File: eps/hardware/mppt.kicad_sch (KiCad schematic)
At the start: 1 part, among them U1 LTC3130IUDC_PBF

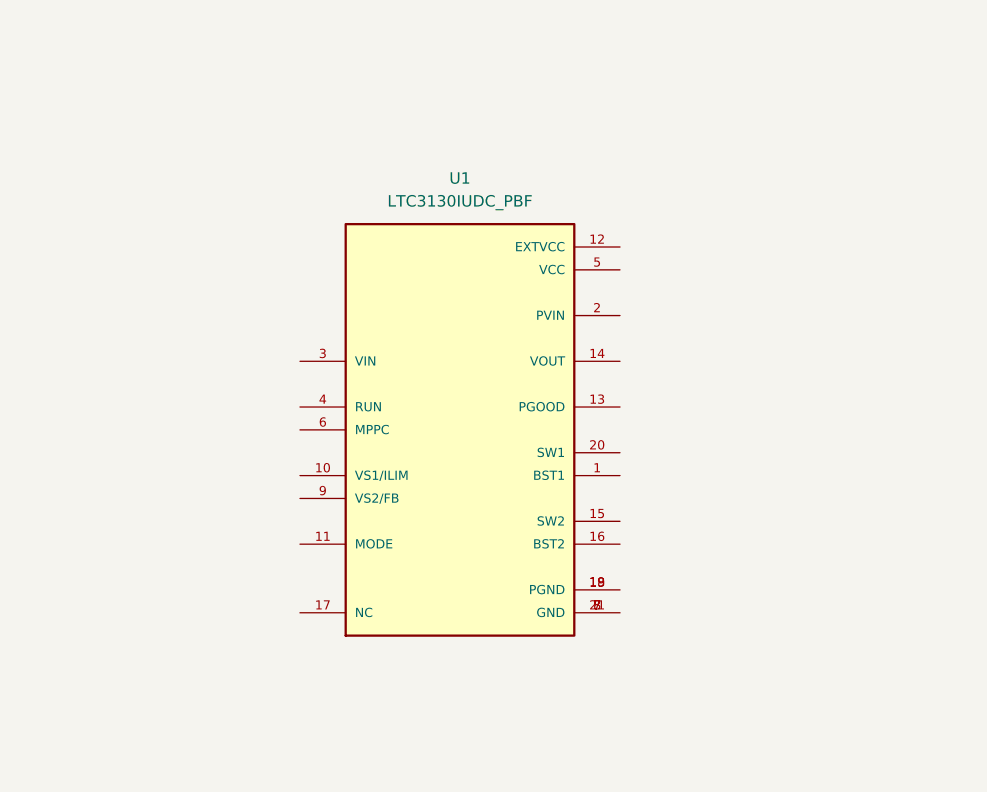
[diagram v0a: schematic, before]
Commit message: begin implementing battery charger
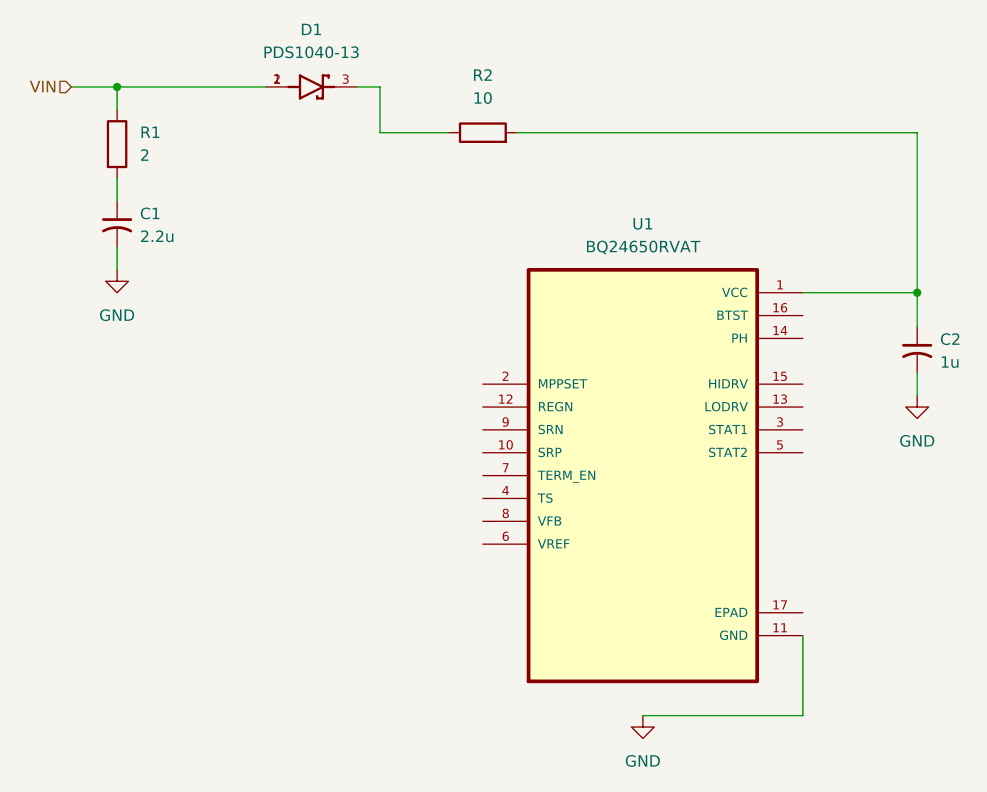
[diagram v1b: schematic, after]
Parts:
- removed U1: LTC3130IUDC_PBF, LTC3130IUDC_PBF:QFN50P400X300X80-21N, symbol LTC3130IUDC_PBF:LTC3130IUDC_PBF
- added C1: 2.2u, Capacitor_SMD:C_0603_1608Metric_Pad1.08x0.95mm_HandSolder, symbol Device:C_Small_US
- added C2: 1u, Capacitor_SMD:C_0603_1608Metric_Pad1.08x0.95mm_HandSolder, symbol Device:C_Small_US
- added D1: PDS1040-13, PDS1040-13:DIO_PDS1040-13, symbol PDS1040-13:PDS1040-13
- added R1: 2, Resistor_SMD:R_0603_1608Metric_Pad0.98x0.95mm_HandSolder, symbol Device:R
- added R2: 10, Resistor_SMD:R_0603_1608Metric_Pad0.98x0.95mm_HandSolder, symbol Device:R
- added U1: BQ24650RVAT, BQ24650RVAT:QFN50P350X350X100-17N, symbol BQ24650RVAT:BQ24650RVAT
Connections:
- new net: C1.1, R1.2
- new net: C2.1, R2.2, U1.1 (VCC)
- new net: D1.3, R2.1
- new net GND: C1.2, C2.2, U1.11 (GND)
- new net VIN: D1.1, D1.2, R1.1
